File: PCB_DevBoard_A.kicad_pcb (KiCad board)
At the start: 2 copper layers, 83 x 71 mm, 55 parts, among them J1 Interconnect B, J2 Interconnect A, J3 Debug, J5 I/O A, J6 I/O B, SW1 SW_DPST_x2, U1 TLV1117-33, U2 XMC1404_F064, U3 TLE7251, U4 ULN2003A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

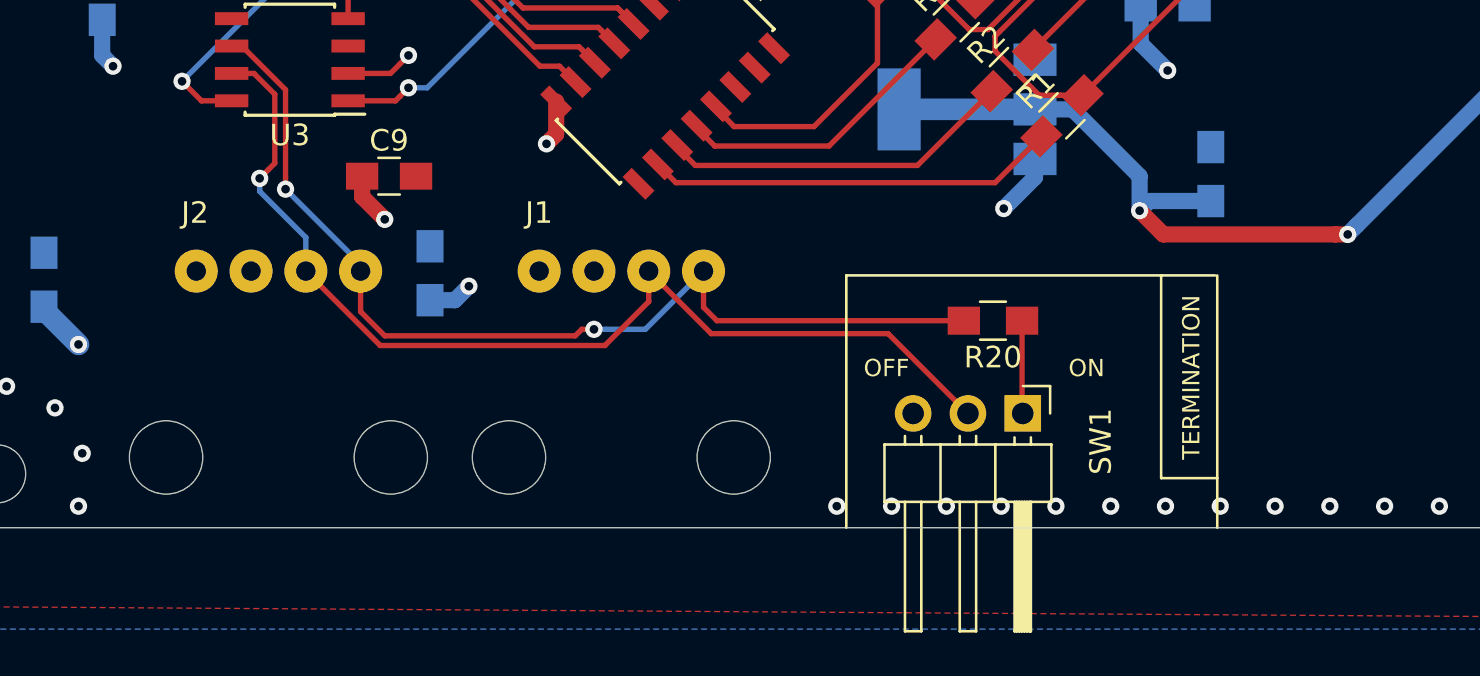
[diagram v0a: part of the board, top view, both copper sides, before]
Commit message: Change the Wolley connectors to the new 5-pin one
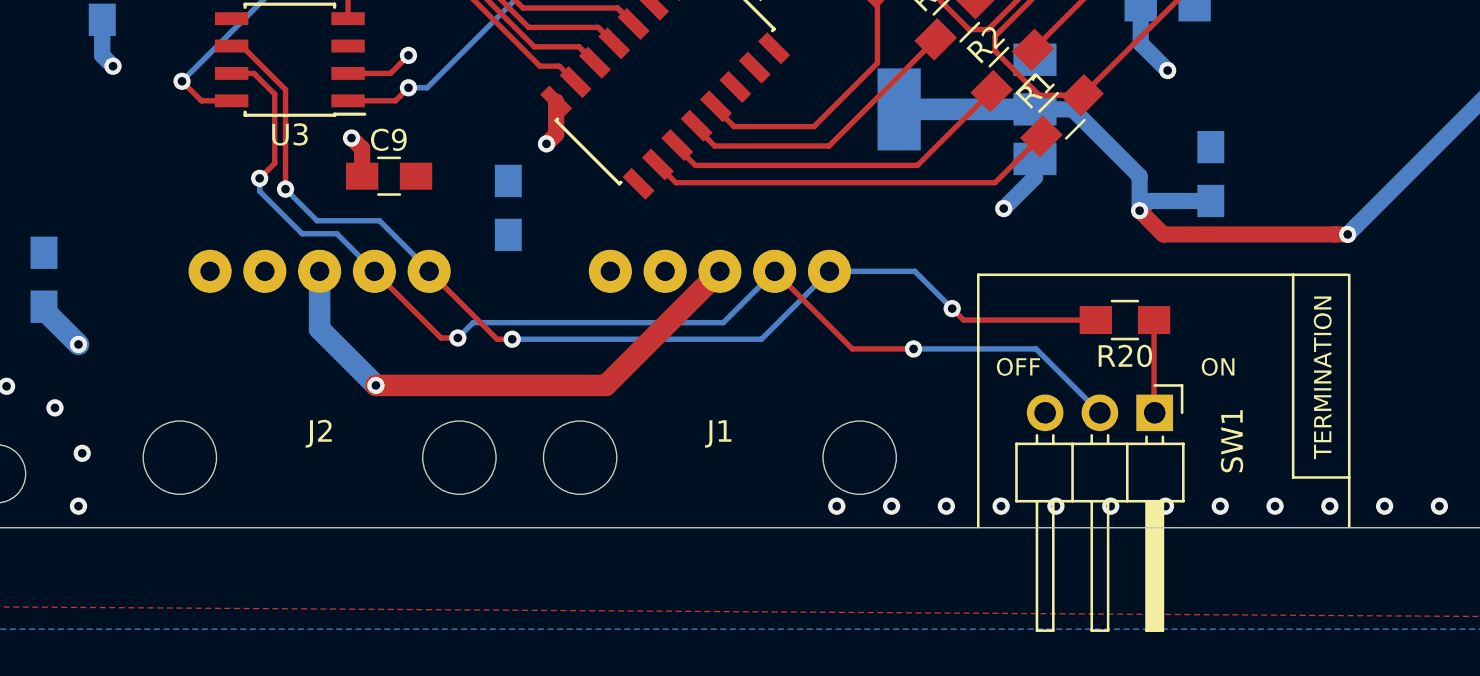
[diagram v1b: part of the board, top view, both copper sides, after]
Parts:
- J1: value Interconnect B -> Conn_01x05; footprint DevBoard:WolletInterconnect_THT_Angeled -> DevBoard:WolleyInterconnect_THT_Angeled
- J2: value Interconnect A -> Conn_01x05; footprint DevBoard:WolletInterconnect_THT_Angeled -> DevBoard:WolleyInterconnect_THT_Angeled
- moved R20 6.12 mm to (166.7, 163.2)
- moved SW1 6.12 mm to (168.1, 167.5)
- moved J1 5.84 mm to (147.9, 160.9)
- moved C15 4.73 mm to (138.1, 158.0)
- moved J2 3.18 mm to (129.4, 160.9)
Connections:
- C14 pad 1: +5V -> GND
- C14 pad 2: GND -> +5V
- J1 pad 3: +5V -> +BATT
- J1 pad 4: GND -> +5V
- J2 pad 3: +5V -> +BATT
- J2 pad 4: GND -> +5V
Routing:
- net +BATT: track 0.00 -> 24.5 mm, vias 0 -> 1
- net +5V: track 57.7 -> 53.3 mm, vias 8 -> 6
- net CAN+: track 48.9 -> 53.0 mm, vias 1 -> 3
- net CAN-: track 46.7 -> 50.7 mm, vias 2 -> 3
- net GND: track 63.3 -> 65.1 mm, vias 121 -> 122

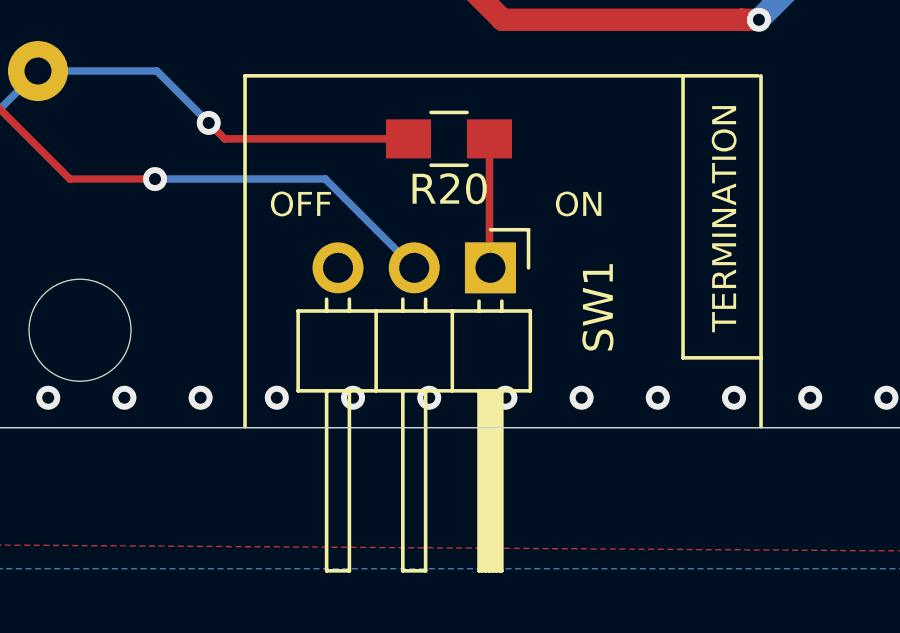
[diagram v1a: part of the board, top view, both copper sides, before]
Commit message: Replace the termination switch with a jumper
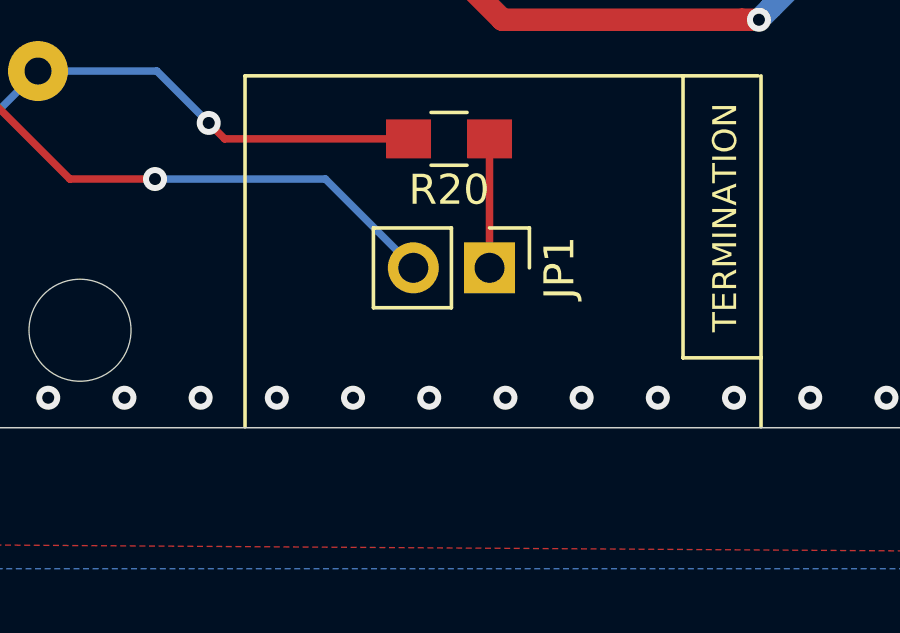
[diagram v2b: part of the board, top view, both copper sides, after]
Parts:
- removed SW1: SW_DPST_x2, Pin_Headers:Pin_Header_Angled_1x03_Pitch2.54mm
- added JP1: Bus Termination, Connector_PinHeader_2.54mm:PinHeader_1x02_P2.54mm_Vertical, F.Cu at (168.1, 167.5)
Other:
- board text removed: "OFF"
- board text removed: "ON"

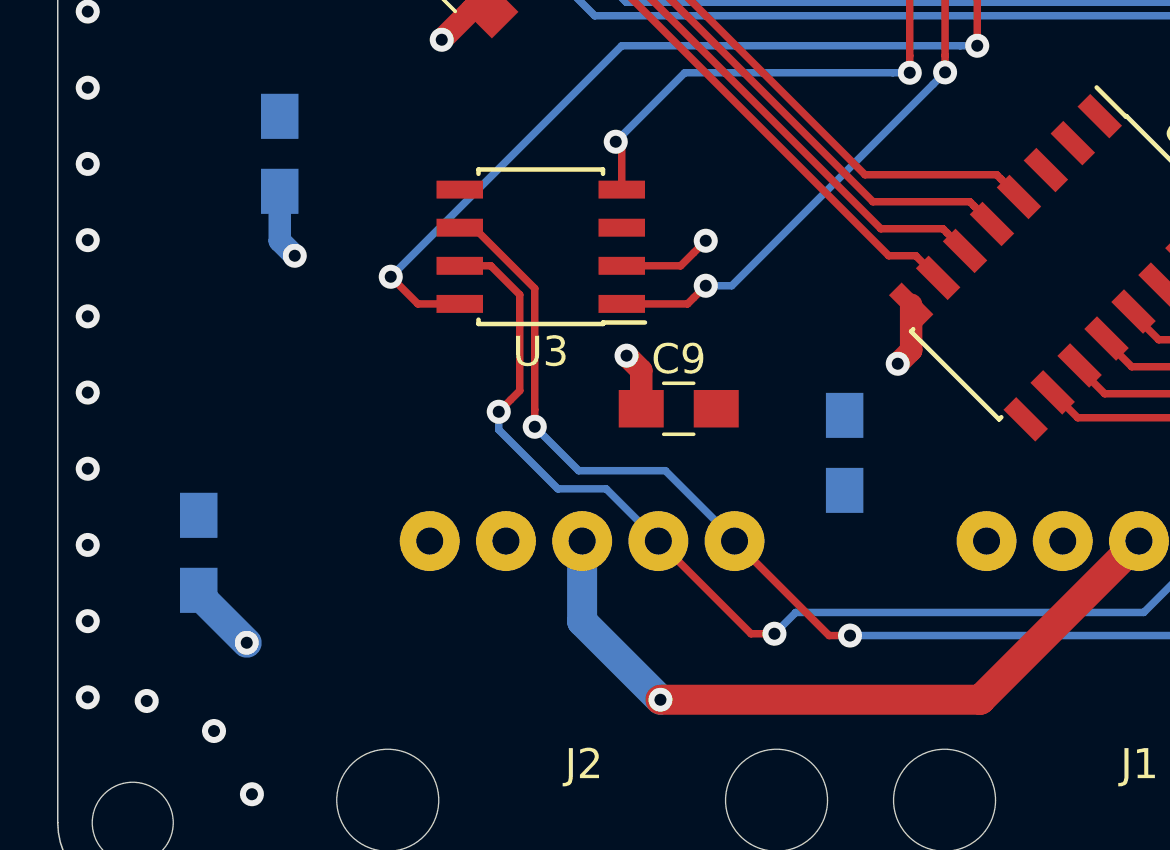
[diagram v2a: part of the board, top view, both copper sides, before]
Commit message: Move some capacitors to a better location
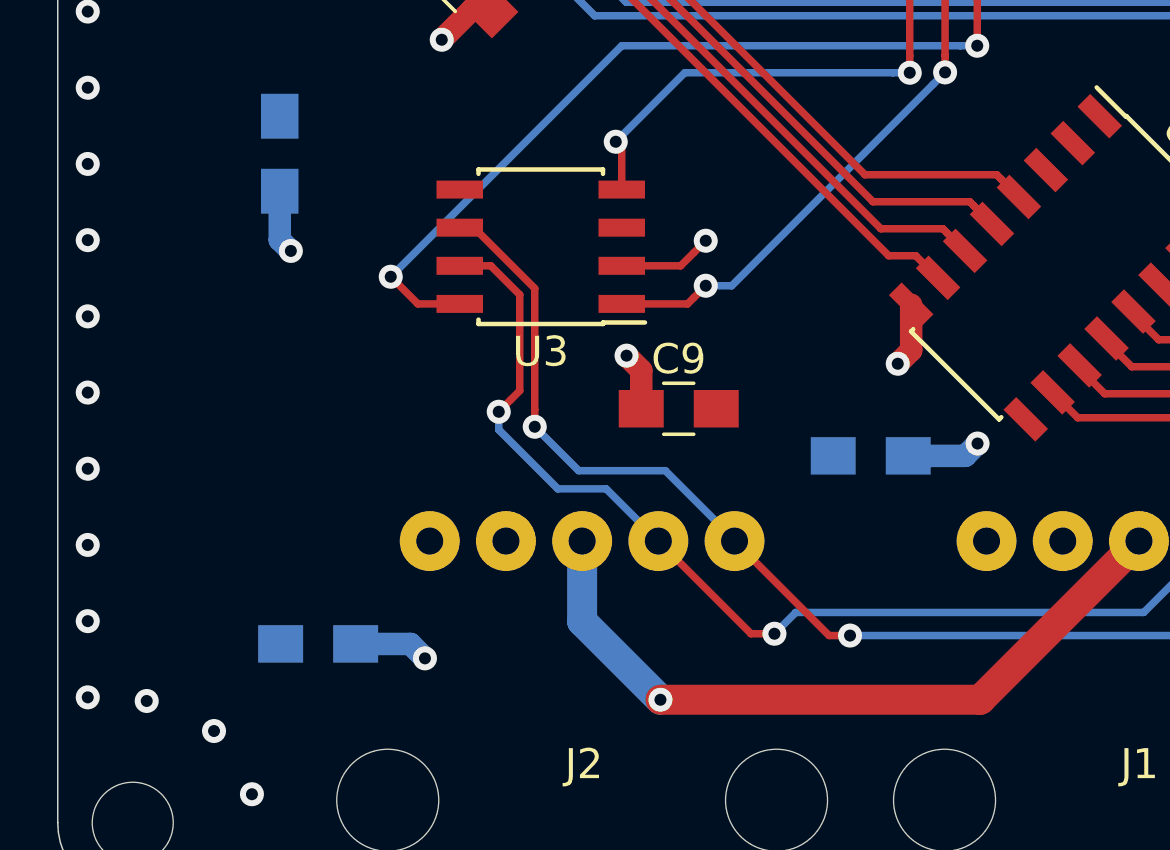
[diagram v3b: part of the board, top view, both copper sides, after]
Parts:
- moved C14 5.01 mm to (120.6, 164.3), turned to 0 degrees
- moved C15 0.88 mm to (139.0, 158.1), turned to 180 degrees
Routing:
- net +5V: track 53.3 -> 58.1 mm, vias 6 -> 8
- net GND: track 65.1 -> 62.8 mm, vias 122 -> 121
